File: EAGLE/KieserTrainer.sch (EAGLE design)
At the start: 11 parts, among them U1 ATMEGA328P-PU

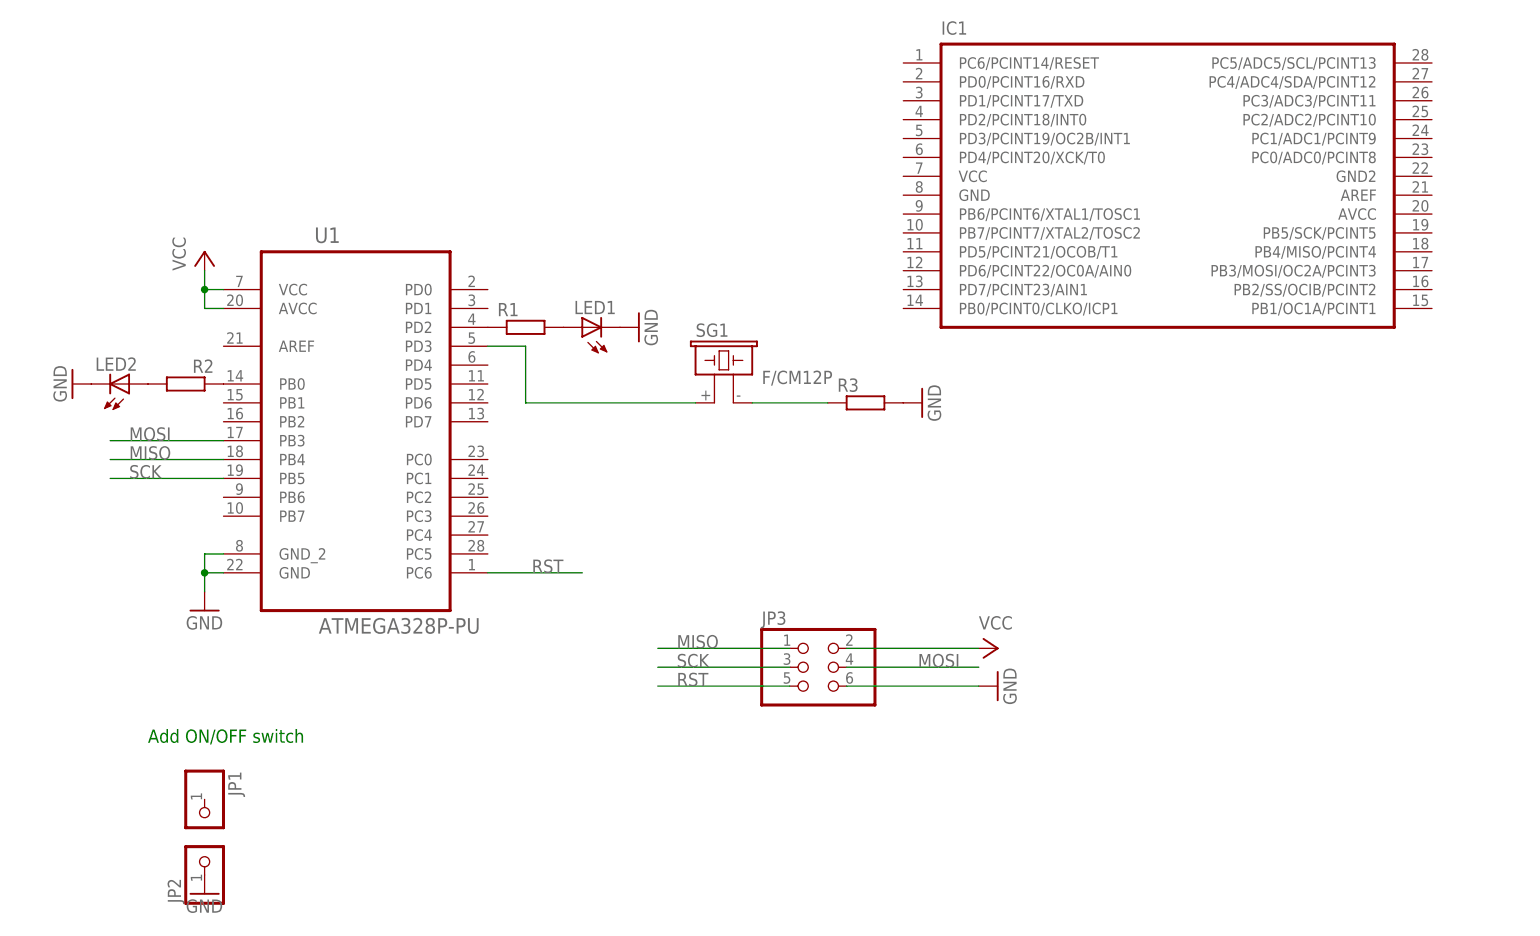
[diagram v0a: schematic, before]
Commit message: Update schematic to match PCB
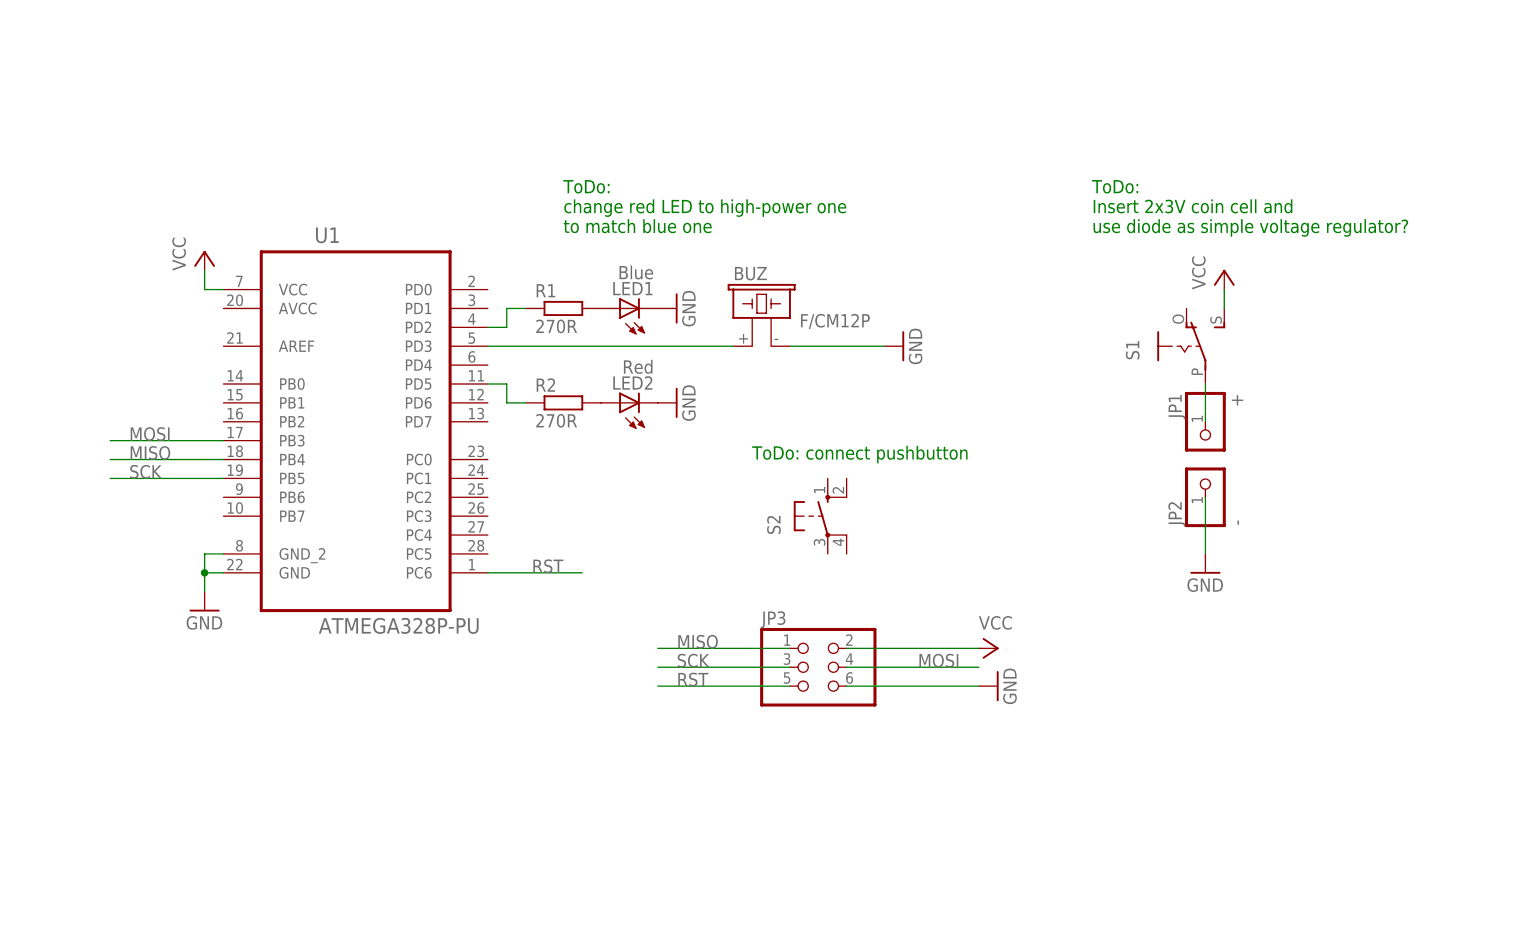
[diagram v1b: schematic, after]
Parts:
- removed IC1: (no value), dp_devices:IC_UC_ATMEGA328PDIL
- removed R3: (no value), rcl:R-EU_R0805
- removed SG1: F/CM12P, buzzer:F/CM12P
- added BUZ: F/CM12P, buzzer:F/CM12P
- added S1: (no value), adafruit:EG1218S
- added S2: (no value), adafruit:40-XX
- JP1: value (none) -> +
- JP2: value (none) -> -
- LED1: value (none) -> Blue
- LED2: value (none) -> Red
- R1, R2: value (none) -> 270R
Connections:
- removed net N$6: R3.1, SG1.2
- new net N$7: JP1.1, S1.P
- net GND: now also BUZ.2; no longer R3.2
- net N$1: now also U1.PD5; no longer U1.PB0
- net N$5: now also BUZ.1; no longer SG1.1
- net VCC: now also S1.S; no longer U1.AVCC
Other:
- note added: "ToDo: Insert 2x3V coin cell and use diode as simple voltage regulator?"
- note added: "ToDo: change red LED to high-power one to match blue one"
- note added: "ToDo: connect pushbutton"
- note removed: "Add ON/OFF switch"
- moved on the sheet: JP1, JP2, LED1, LED2, R1, R2
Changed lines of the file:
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@@
 <parts>
 <part name="U1" library="Atmel_By_element14_Batch_1-00" deviceset="ATMEGA328P-PU" device=""/>
-<part name="SG1" library="buzzer" deviceset="F/CM12P" device=""/>
-<part name="LED1" library="adafruit" deviceset="LED" device="CHIPLED_0805"/>
-<part name="LED2" library="adafruit" deviceset="LED" device="CHIPLED_0805"/>
-<part name="R1" library="rcl" deviceset="R-EU_" device="R0805"/>
-<part name="R2" library="rcl" deviceset="R-EU_" device="R0805"/>
-<part name="JP1" library="pinhead" deviceset="PINHD-1X1" device=""/>
-<part name="JP2" library="pinhead" deviceset="PINHD-1X1" device=""/>
+<part name="BUZ" library="buzzer" deviceset="F/CM12P" device=""/>
+<part name="LED1" library="adafruit" deviceset="LED" device="CHIPLED_0805" value="Blue"/>
+<part name="LED2" library="adafruit" deviceset="LED" device="CHIPLED_0805" value="Red"/>
+<part name="R1" library="rcl" deviceset="R-EU_" device="R0805" value="270R"/>
+<part name="R2" library="rcl" deviceset="R-EU_" device="R0805" value="270R"/>
+<part name="JP1" library="pinhead" deviceset="PINHD-1X1" device="" value="+"/>
+<part name="JP2" library="pinhead" deviceset="PINHD-1X1" device="" value="-"/>
 <part name="GND1" library="supply1" deviceset="GND" device=""/>
 <part name="GND2" library="supply1" deviceset="GND" device=""/>
@@
 <part name="GND4" library="supply1" deviceset="GND" device=""/>
 <part name="P+1" library="supply1" deviceset="VCC" device=""/>
-<part name="R3" library="rcl" deviceset="R-EU_" device="R0805"/>
 <part name="GND5" library="supply1" deviceset="GND" device=""/>
 <part name="JP3" library="pinhead" deviceset="PINHD-2X3" device=""/>
-<part name="IC1" library="dp_devices" deviceset="IC_UC_ATMEGA328P" device="DIL"/>
 <part name="P+2" library="supply1" deviceset="VCC" device=""/>
 <part name="GND6" library="supply1" deviceset="GND" device=""/>
+<part name="S1" library="adafruit" deviceset="EG1218" device="S"/>
+<part name="S2" library="adafruit" deviceset="40-XX" device=""/>
+<part name="P+3" library="supply1" deviceset="VCC" device=""/>
 </parts>
 <sheets>
 <sheet>
 <plain>
-<text x="22.86" y="15.24" size="1.778" layer="91">Add ON/OFF switch</text>
+<text x="104.14" y="53.34" size="1.778" layer="91">ToDo: connect pushbutton</text>
+<text x="78.74" y="83.82" size="1.778" layer="91">ToDo:
+change red LED to high-power one
+to match blue one</text>
+<text x="149.86" y="83.82" size="1.778" layer="91">ToDo:
+Insert 2x3V coin cell and
+use diode as simple voltage regulator?</text>
 </plain>
 <instances>
 <instance part="U1" gate="A" x="50.8" y="60.96"/>
-<instance part="SG1" gate="G$1" x="99.06" y="63.5"/>
-<instance part="LED1" gate="G$1" x="81.28" y="71.12" rot="R90"/>
-<instance part="LED2" gate="G$1" x="20.32" y="63.5" rot="MR90"/>
-<instance part="R1" gate="G$1" x="73.66" y="71.12"/>
-<instance part="R2" gate="G$1" x="27.94" y="63.5" rot="MR0"/>
-<instance part="JP1" gate="G$1" x="30.48" y="5.08" rot="R270"/>
-<instance part="JP2" gate="G$1" x="30.48" y="0" rot="R90"/>
-<instance part="GND1" gate="1" x="88.9" y="71.12" rot="R90"/>
-<instance part="GND2" gate="1" x="12.7" y="63.5" rot="R270"/>
-<instance part="GND3" gate="1" x="30.48" y="-5.08"/>
+<instance part="BUZ" gate="G$1" x="104.14" y="71.12"/>
+<instance part="LED1" gate="G$1" x="86.36" y="73.66" rot="R90"/>
+<instance part="LED2" gate="G$1" x="86.36" y="60.96" rot="R90"/>
+<instance part="R1" gate="G$1" x="78.74" y="73.66"/>
+<instance part="R2" gate="G$1" x="78.74" y="60.96"/>
+<instance part="JP1" gate="G$1" x="165.1" y="55.88" rot="MR270"/>
+<instance part="JP2" gate="G$1" x="165.1" y="50.8" rot="R90"/>
+<instance part="GND1" gate="1" x="93.98" y="73.66" rot="R90"/>
+<instance part="GND2" gate="1" x="93.98" y="60.96" rot="R90"/>
+<instance part="GND3" gate="1" x="165.1" y="38.1"/>
 <instance part="GND4" gate="1" x="30.48" y="33.02"/>
 <instance part="P+1" gate="VCC" x="30.48" y="81.28"/>
-<instance part="R3" gate="G$1" x="119.38" y="60.96"/>
-<instance part="GND5" gate="1" x="127" y="60.96" rot="R90"/>
+<instance part="GND5" gate="1" x="124.46" y="68.58" rot="R90"/>
 <instance part="JP3" gate="A" x="111.76" y="25.4"/>
-<instance part="IC1" gate="G$1" x="160.02" y="91.44"/>
 <instance part="P+2" gate="VCC" x="137.16" y="27.94" rot="R270"/>
 <instance part="GND6" gate="1" x="137.16" y="22.86" rot="R90"/>
+<instance part="S1" gate="1" x="162.56" y="68.58"/>
+<instance part="S2" gate="1" x="114.3" y="45.72"/>
+<instance part="P+3" gate="VCC" x="167.64" y="78.74"/>
 </instances>
 <busses>
@@
 <pinref part="JP2" gate="G$1" pin="1"/>
 <pinref part="GND3" gate="1" pin="GND"/>
+<wire x1="165.1" y1="40.64" x2="165.1" y2="48.26" width="0.1524" layer="91"/>
 </segment>
 <segment>
@@
 </segment>
 <segment>
-<pinref part="R3" gate="G$1" pin="2"/>
-<pinref part="GND5" gate="1" pin="GND"/>
-</segment>
-<segment>
 <pinref part="GND1" gate="1" pin="GND"/>
 <pinref part="LED1" gate="G$1" pin="C"/>
@@
 <wire x1="116.84" y1="22.86" x2="134.62" y2="22.86" width="0.1524" layer="91"/>
 <pinref part="GND6" gate="1" pin="GND"/>
+</segment>
+<segment>
+<pinref part="BUZ" gate="G$1" pin="2"/>
+<wire x1="121.92" y1="68.58" x2="109.22" y2="68.58" width="0.1524" layer="91"/>
+<pinref part="GND5" gate="1" pin="GND"/>
 </segment>
 </net>
@@
 <wire x1="30.48" y1="78.74" x2="30.48" y2="76.2" width="0.1524" layer="91"/>
 <wire x1="33.02" y1="76.2" x2="30.48" y2="76.2" width="0.1524" layer="91"/>
-<pinref part="U1" gate="A" pin="AVCC"/>
-<wire x1="30.48" y1="76.2" x2="30.48" y2="73.66" width="0.1524" layer="91"/>
-<wire x1="30.48" y1="73.66" x2="33.02" y2="73.66" width="0.1524" layer="91"/>
-<junction x="30.48" y="76.2"/>
 </segment>
 <segment>
@@
 <pinref part="P+2" gate="VCC" pin="VCC"/>
 </segment>
-</net>
-<net name="N$6" class="0">
-<segment>
-<pinref part="SG1" gate="G$1" pin="2"/>
-<pinref part="R3" gate="G$1" pin="1"/>
-<wire x1="114.3" y1="60.96" x2="104.14" y2="60.96" width="0.1524" layer="91"/>
-</segment>
-</net>
-<net name="N$1" class="0">
-<segment>
-<pinref part="U1" gate="A" pin="PB0"/>
-<pinref part="R2" gate="G$1" pin="1"/>
+<segment>
+<pinref part="S1" gate="1" pin="S"/>
+<pinref part="P+3" gate="VCC" pin="VCC"/>
+<wire x1="167.64" y1="76.2" x2="167.64" y2="73.66" width="0.1524" layer="91"/>
 </segment>
 </net>
@@
 <pinref part="U1" gate="A" pin="PD2"/>
 <pinref part="R1" gate="G$1" pin="1"/>
+<wire x1="73.66" y1="73.66" x2="71.12" y2="73.66" width="0.1524" layer="91"/>
+<wire x1="71.12" y1="73.66" x2="71.12" y2="71.12" width="0.1524" layer="91"/>
+<wire x1="71.12" y1="71.12" x2="68.58" y2="71.12" width="0.1524" layer="91"/>
 </segment>
 </net>
@@
 <segment>
 <pinref part="U1" gate="A" pin="PD3"/>
-<wire x1="68.58" y1="68.58" x2="73.66" y2="68.58" width="0.1524" layer="91"/>
-<pinref part="SG1" gate="G$1" pin="1"/>
-<wire x1="73.66" y1="68.58" x2="73.66" y2="60.96" width="0.1524" layer="91"/>
-<wire x1="73.66" y1="60.96" x2="96.52" y2="60.96" width="0.1524" layer="91"/>
+<pinref part="BUZ" gate="G$1" pin="1"/>
+<wire x1="68.58" y1="68.58" x2="101.6" y2="68.58" width="0.1524" layer="91"/>
+</segment>
+</net>
+<net name="N$1" class="0">
+<segment>
+<pinref part="U1" gate="A" pin="PD5"/>
+<pinref part="R2" gate="G$1" pin="1"/>
+<wire x1="73.66" y1="60.96" x2="71.12" y2="60.96" width="0.1524" layer="91"/>
+<wire x1="71.12" y1="60.96" x2="71.12" y2="63.5" width="0.1524" layer="91"/>
+<wire x1="71.12" y1="63.5" x2="68.58" y2="63.5" width="0.1524" layer="91"/>
+</segment>
+</net>
+<net name="N$7" class="0">
+<segment>
+<pinref part="JP1" gate="G$1" pin="1"/>
+<pinref part="S1" gate="1" pin="P"/>
+<wire x1="165.1" y1="58.42" x2="165.1" y2="63.5" width="0.1524" layer="91"/>
 </segment>
 </net>
@@
 </schematic>
 </drawing>
+<compatibility>
+<note version="6.3" minversion="6.2.2" severity="warning">
+Since Version 6.2.2 text objects can contain more than one line,
+which will not be processed correctly with this version.
+</note>
+</compatibility>
 </eagle>

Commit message: Make both LEDs blue high-power (brighter!), add 2x mystery diode to make ~5V out of ~6V
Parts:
- added D1, D2: (no value), diode:DIODE-D-7.5
- LED2: value Red -> blue
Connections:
- new net N$6: D1.A, S1.S
- new net N$8: D1.C, D2.A
- net VCC: now also D2.C; no longer S1.S
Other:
- note added: "2x CR2016 3V = 6V"
- note added: "Mystery diodes make ~5V out of 6V"
- note removed: "ToDo: Insert 2x3V coin cell and use diode as simple voltage regulator?"
- note removed: "ToDo: change red LED to high-power one to match blue one"
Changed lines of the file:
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@@
 <part name="BUZ" library="buzzer" deviceset="F/CM12P" device=""/>
 <part name="LED1" library="adafruit" deviceset="LED" device="CHIPLED_0805" value="Blue"/>
-<part name="LED2" library="adafruit" deviceset="LED" device="CHIPLED_0805" value="Red"/>
+<part name="LED2" library="adafruit" deviceset="LED" device="CHIPLED_0805" value="blue"/>
 <part name="R1" library="rcl" deviceset="R-EU_" device="R0805" value="270R"/>
 <part name="R2" library="rcl" deviceset="R-EU_" device="R0805" value="270R"/>
@@
 <part name="S2" library="adafruit" deviceset="40-XX" device=""/>
 <part name="P+3" library="supply1" deviceset="VCC" device=""/>
+<part name="D1" library="diode" deviceset="DIODE-" device="D-7.5"/>
+<part name="D2" library="diode" deviceset="DIODE-" device="D-7.5"/>
 </parts>
 <sheets>
@@
 <plain>
 <text x="104.14" y="53.34" size="1.778" layer="91">ToDo: connect pushbutton</text>
-<text x="78.74" y="83.82" size="1.778" layer="91">ToDo:
-change red LED to high-power one
-to match blue one</text>
-<text x="149.86" y="83.82" size="1.778" layer="91">ToDo:
-Insert 2x3V coin cell and
-use diode as simple voltage regulator?</text>
+<text x="139.7" y="83.82" size="1.778" layer="91">Mystery diodes
+make ~5V out of 6V</text>
+<text x="157.48" y="40.64" size="1.778" layer="91" rot="R90">2x CR2016 3V = 6V</text>
 </plain>
 <instances>
@@
 <instance part="S1" gate="1" x="162.56" y="68.58"/>
 <instance part="S2" gate="1" x="114.3" y="45.72"/>
-<instance part="P+3" gate="VCC" x="167.64" y="78.74"/>
+<instance part="P+3" gate="VCC" x="167.64" y="99.06"/>
+<instance part="D1" gate="G$1" x="167.64" y="78.74" rot="R90"/>
+<instance part="D2" gate="G$1" x="167.64" y="88.9" rot="R90"/>
 </instances>
 <busses>
@@
 </segment>
 <segment>
-<pinref part="S1" gate="1" pin="S"/>
+<pinref part="D2" gate="G$1" pin="C"/>
 <pinref part="P+3" gate="VCC" pin="VCC"/>
-<wire x1="167.64" y1="76.2" x2="167.64" y2="73.66" width="0.1524" layer="91"/>
+<wire x1="167.64" y1="96.52" x2="167.64" y2="91.44" width="0.1524" layer="91"/>
 </segment>
 </net>
@@
 </segment>
 </net>
+<net name="N$6" class="0">
+<segment>
+<pinref part="S1" gate="1" pin="S"/>
+<pinref part="D1" gate="G$1" pin="A"/>
+<wire x1="167.64" y1="76.2" x2="167.64" y2="73.66" width="0.1524" layer="91"/>
+</segment>
+</net>
+<net name="N$8" class="0">
+<segment>
+<pinref part="D1" gate="G$1" pin="C"/>
+<pinref part="D2" gate="G$1" pin="A"/>
+<wire x1="167.64" y1="86.36" x2="167.64" y2="81.28" width="0.1524" layer="91"/>
+</segment>
+</net>

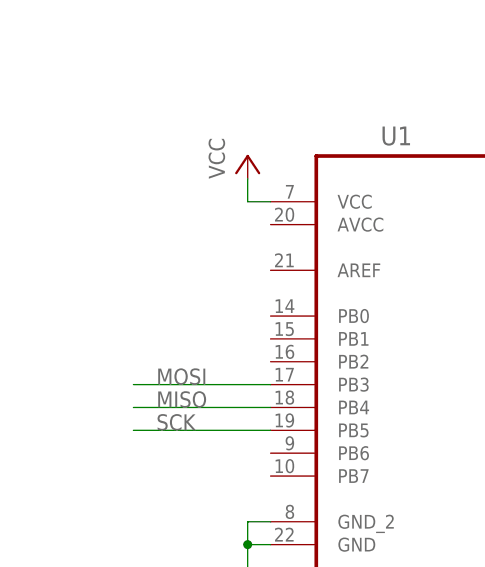
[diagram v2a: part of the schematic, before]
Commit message: Add bypass capactior on uC supply pins
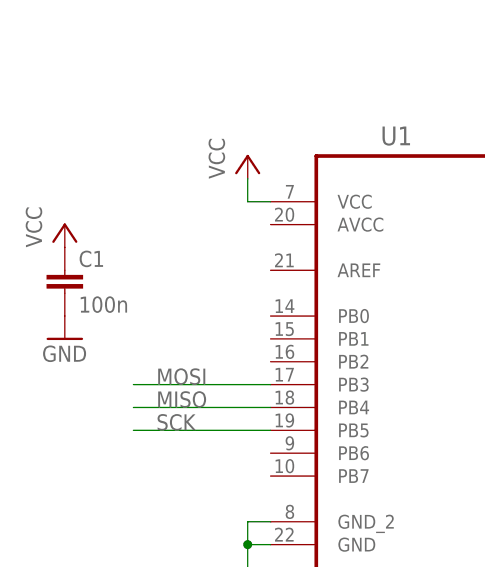
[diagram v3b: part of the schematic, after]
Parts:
- added C1: 100n, rcl:C-EUC0805
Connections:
- net GND: now also C1.2
- net VCC: now also C1.1
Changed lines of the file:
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@@
 <part name="D1" library="diode" deviceset="DIODE-" device="D-7.5"/>
 <part name="D2" library="diode" deviceset="DIODE-" device="D-7.5"/>
+<part name="C1" library="rcl" deviceset="C-EU" device="C0805" value="100n"/>
+<part name="P+4" library="supply1" deviceset="VCC" device=""/>
+<part name="GND7" library="supply1" deviceset="GND" device=""/>
 </parts>
 <sheets>
@@
 <instance part="D1" gate="G$1" x="167.64" y="78.74" rot="R90"/>
 <instance part="D2" gate="G$1" x="167.64" y="88.9" rot="R90"/>
+<instance part="C1" gate="G$1" x="10.16" y="68.58"/>
+<instance part="P+4" gate="VCC" x="10.16" y="73.66"/>
+<instance part="GND7" gate="1" x="10.16" y="60.96"/>
 </instances>
 <busses>
@@
 <pinref part="GND5" gate="1" pin="GND"/>
 </segment>
+<segment>
+<pinref part="C1" gate="G$1" pin="2"/>
+<pinref part="GND7" gate="1" pin="GND"/>
+</segment>
 </net>
 <net name="VCC" class="0">
@@
 <wire x1="167.64" y1="96.52" x2="167.64" y2="91.44" width="0.1524" layer="91"/>
 </segment>
+<segment>
+<pinref part="C1" gate="G$1" pin="1"/>
+<pinref part="P+4" gate="VCC" pin="VCC"/>
+</segment>
 </net>
